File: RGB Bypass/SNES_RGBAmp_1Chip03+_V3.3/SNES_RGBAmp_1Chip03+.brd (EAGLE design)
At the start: 31.1 x 20.5 mm, 30 parts

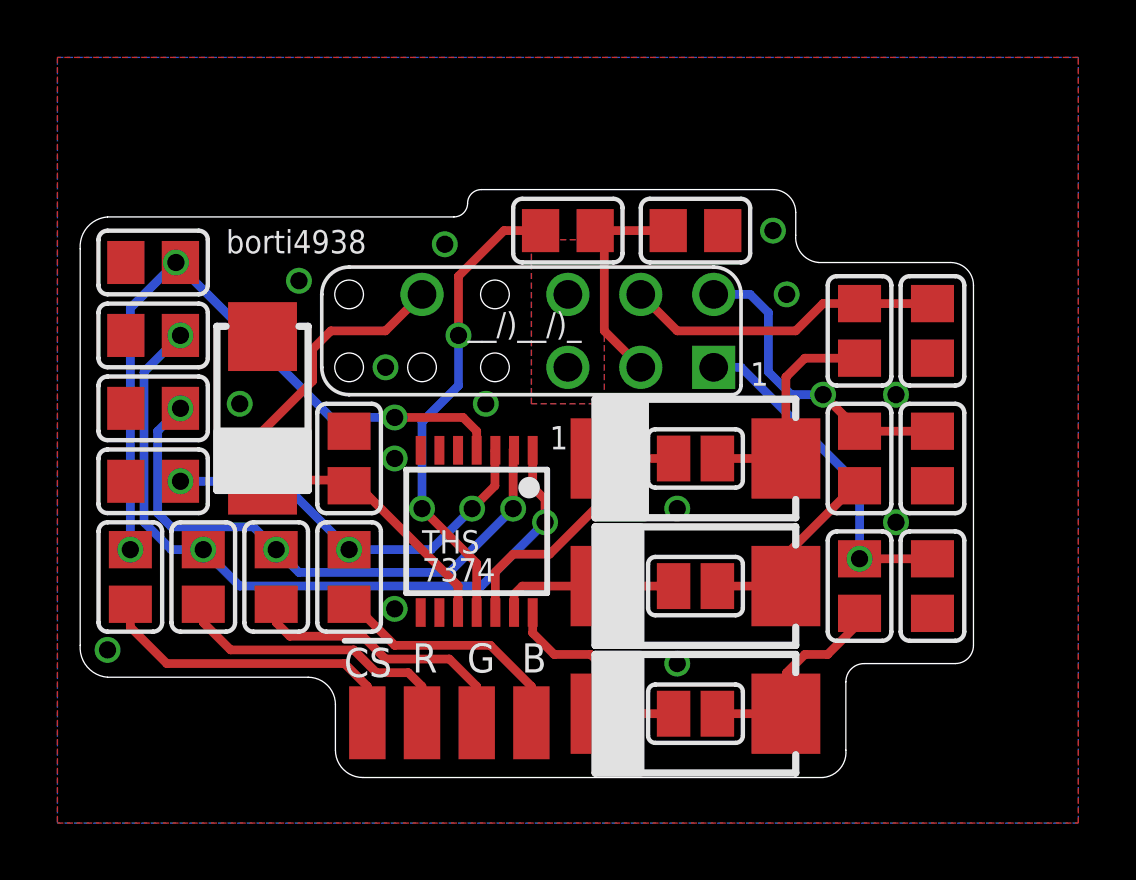
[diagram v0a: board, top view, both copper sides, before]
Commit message: Update: 330uF tantalum in CSYNC line at the output of the THS7374.
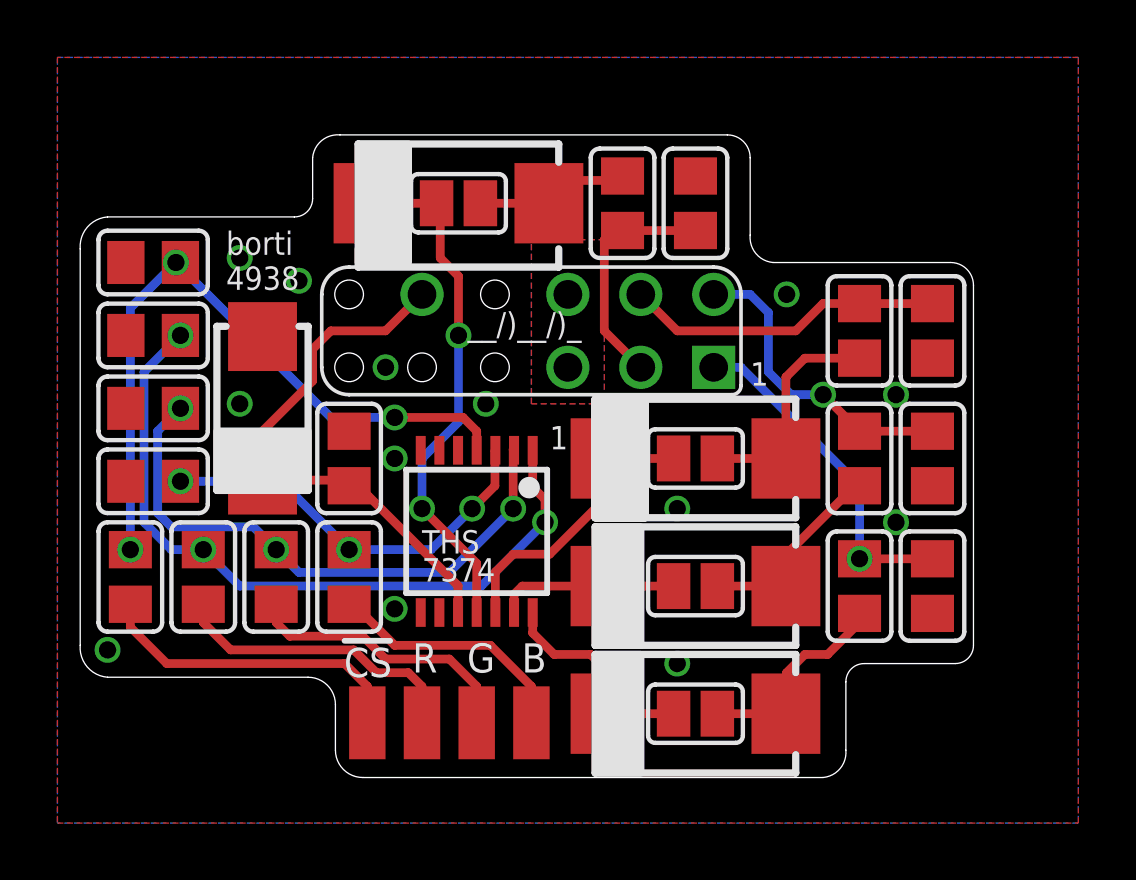
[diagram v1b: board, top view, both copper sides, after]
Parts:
- added C10: 330u, rcl:SMC_D
- added SJ4: (no value), jumper:SJ
- moved R15 2.13 mm to (29.8, 43.2), turned to 270 degrees
- moved C7 0.95 mm to (32.4, 43.2), turned to 90 degrees
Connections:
- new net N$19: C10.-, R15.1, SJ4.2
- net N$18: now also C10.+, SJ4.1; no longer R15.1
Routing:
- net N$19: track 0.00 -> 5.80 mm
- net N$18: track 16.5 -> 18.3 mm
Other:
- board size 31.1 x 20.5 mm -> 31.1 x 22.4 mm
- board text added: "C6 (330uF/ 6.3V )"
- board text added: "borti 4938"
- board text removed: "borti4938"

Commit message: Update silkscreen
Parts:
- removed R13, R14, R15: 75, snescart:Z0805
- added R7: 9.53k, snescart:Z0805
- added R8, R9: 8.45k, snescart:Z0805
- C10: value 330u -> 47p; device rcl:SMC_D -> snescart:Z0805
- C6: value 100n -> 330u; device snescart:Z0805 -> rcl:SMC_D
- C7, C8, C9: value 100n -> 47p
- R10: value 75 -> 75-421
- R11: value 75 -> 5.0k
- R12: value 75 -> 4.3k
- R4: value 75 -> 806
- R5, R6: value 75 -> 1.3k
- moved C6 21.2 mm to (24.1, 43.2), turned to 0 degrees
- moved R10 19.6 mm to (29.8, 43.2)
- moved C7 15.7 mm to (40.6, 29.8), turned to 270 degrees
- moved R12 12.9 mm to (13.5, 41.1), turned to 0 degrees
- moved R6 10.8 mm to (20.3, 30.2), turned to 270 degrees
- moved R1 8.89 mm to (38.1, 29.8)
- moved C10 8.25 mm to (32.4, 43.2), turned to 90 degrees
- moved R5 7.27 mm to (17.8, 30.2), turned to 270 degrees
- moved R11 5.08 mm to (12.7, 30.2)
- moved R2 4.45 mm to (38.1, 34.3)
- moved R3 4.45 mm to (38.1, 38.7)
- moved R4 3.76 mm to (15.2, 30.2), turned to 270 degrees
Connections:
- removed net N$3: R12.1, R4.2, U$2.3
- new net R9: R6.1, R9.2, U$2.3
- net GND: now also C10.2, R12.1, R7.1, R8.1, R9.1; no longer C6.2, R14.1, R4.1, R5.1, R6.1
- net N$1: now also R4.1, R7.2; no longer R10.1, R6.2
- net N$10: now also R11.1, R12.2; no longer R13.1, R14.2
- net N$13: now also R2.1; no longer R3.1
- net N$14: now also R4.2; no longer R10.2
- net N$15: now also R5.2; no longer R11.2
- net N$16: now also R6.2; no longer R12.2
- net N$17: now also R11.2; no longer R13.2
- net N$18: now also C6.+; no longer C10.+
- net N$19: now also C6.-, R10.1; no longer C10.-, R15.1
- net N$2: now also R5.1, R8.2; no longer R11.1, R5.2
- net N$20: now also C10.1, R10.2; no longer C7.1, R15.2
- net N$4: now also R1.1; no longer R2.1
- net N$5: now also C7.1, R1.2; no longer C6.1, R2.2
- net N$6: now also R2.2; no longer R3.2
- net N$8: now also R3.1; no longer R1.1
- net N$9: now also R3.2; no longer R1.2
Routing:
- net R9: track 0.00 -> 14.8 mm, vias 0 -> 3
- net N$3: track 14.8 -> 0.00 mm, vias 3 -> 0
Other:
- board text added: "(75Ω- 421Ω)"
- board text added: "+"
- board text removed: "(75Ω- 300Ω)"

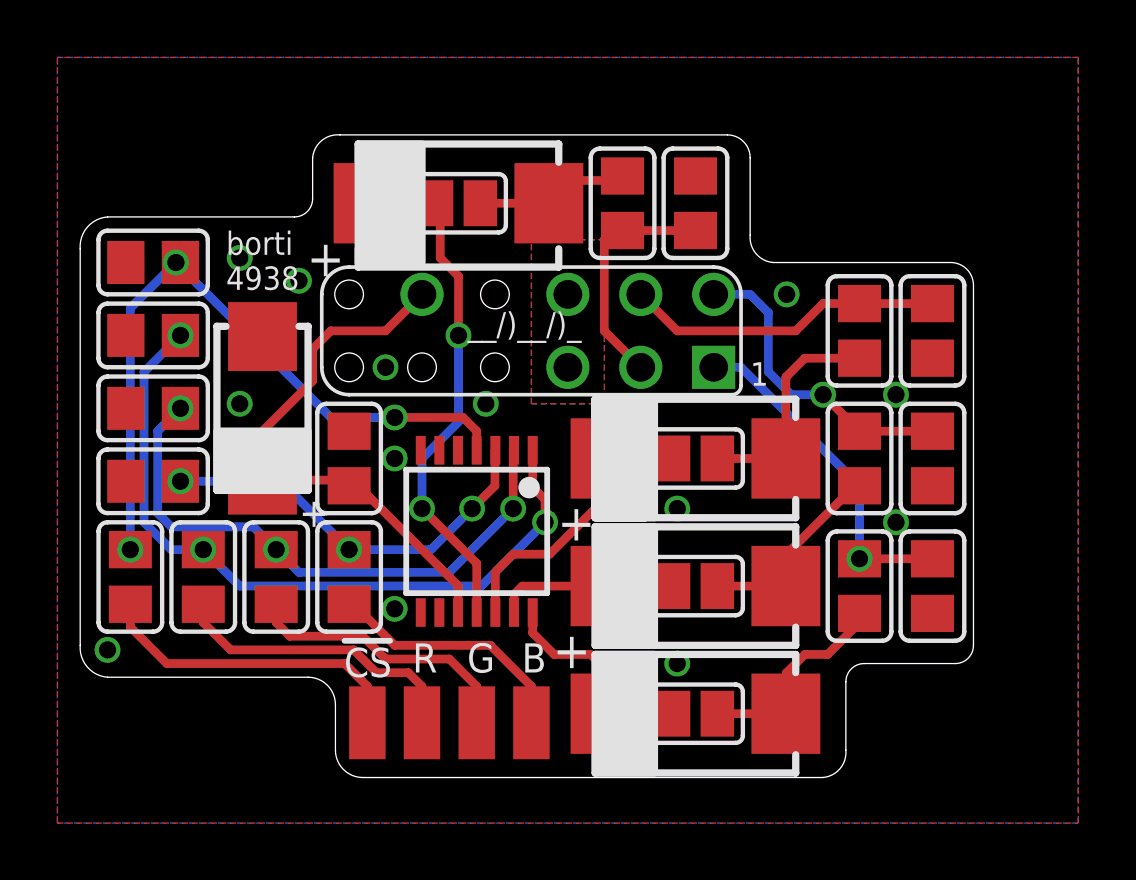
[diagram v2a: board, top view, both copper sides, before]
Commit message: move R12 to avoid a slight overlapping between the PCB and a mounting screw in SNES Mini and SFC Jr.
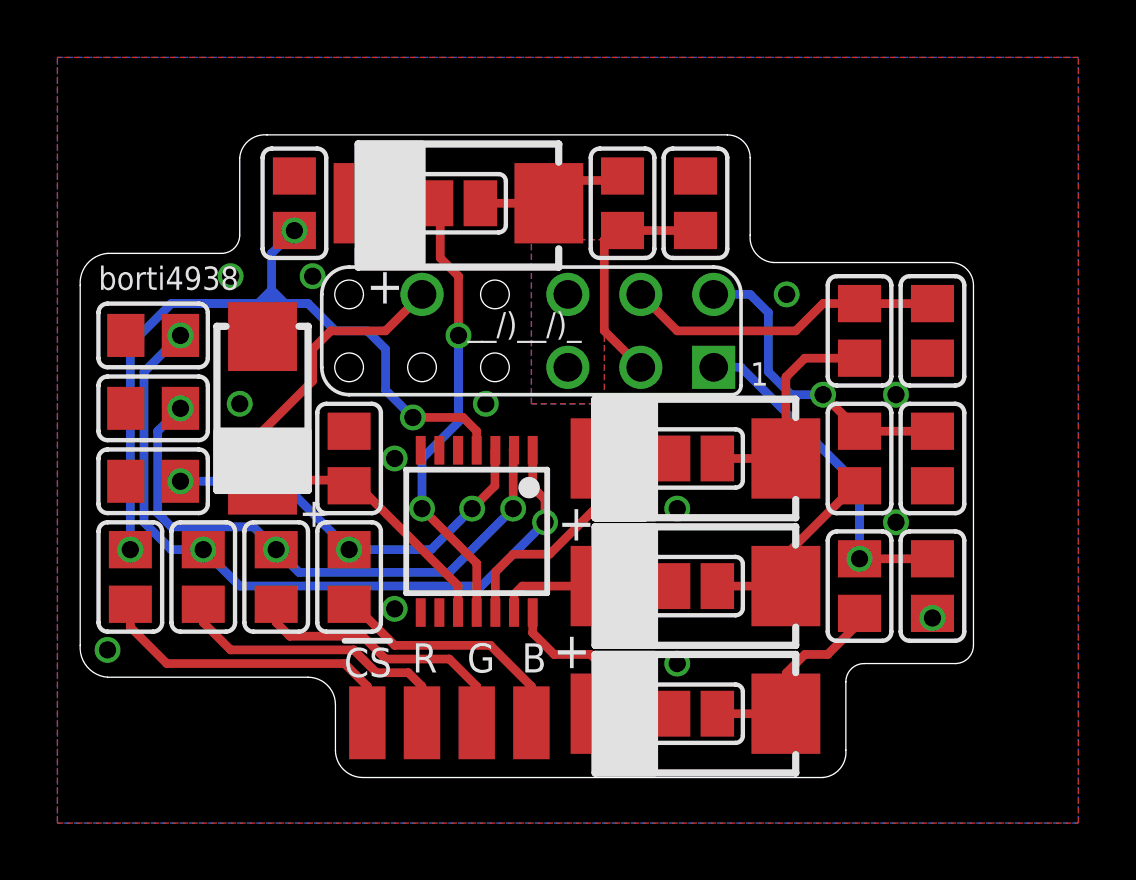
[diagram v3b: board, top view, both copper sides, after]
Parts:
- moved R12 5.34 mm to (18.4, 43.2), turned to 270 degrees
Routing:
- net N$10: track 24.6 -> 27.6 mm
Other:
- outline, holes or cut-outs redrawn
- board text added: "borti4938"
- board text removed: "borti 4938"
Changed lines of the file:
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@@
 <text x="30.95625" y="33.9725" size="1.016" layer="22" font="vector" ratio="12" rot="MR0">RGBAmp for
 SNES V3.3b</text>
-<wire x1="11.90625" y1="42.70375" x2="10.95375" y2="41.5925" width="0" layer="20" curve="90"/>
-<wire x1="10.95375" y1="41.5925" x2="10.95375" y2="27.78125" width="0" layer="20"/>
+<wire x1="11.90625" y1="41.43375" x2="10.95375" y2="40.3225" width="0" layer="20" curve="90"/>
+<wire x1="10.95375" y1="40.3225" x2="10.95375" y2="27.78125" width="0" layer="20"/>
 <wire x1="10.95375" y1="27.78125" x2="11.90625" y2="26.67" width="0" layer="20" curve="90"/>
 <wire x1="11.90625" y1="26.67" x2="18.89125" y2="26.67" width="0" layer="20"/>
@@
 <wire x1="41.43375" y1="27.14625" x2="42.06875" y2="27.78125" width="0" layer="20" curve="90"/>
 <text x="18.57375" y="31.90875" size="1.016" layer="21" font="vector" ratio="15" distance="20">+</text>
-<wire x1="11.90625" y1="42.70375" x2="18.415" y2="42.70375" width="0" layer="20"/>
-<wire x1="20.0025" y1="45.56125" x2="33.49625" y2="45.56125" width="0" layer="20"/>
+<wire x1="11.90625" y1="41.43375" x2="15.875" y2="41.43375" width="0" layer="20"/>
+<wire x1="17.4625" y1="45.56125" x2="33.49625" y2="45.56125" width="0" layer="20"/>
 <wire x1="33.49625" y1="45.56125" x2="34.29" y2="44.7675" width="0" layer="20" curve="-90"/>
 <wire x1="34.29" y1="44.7675" x2="34.29" y2="42.06875" width="0" layer="20"/>
@@
 <text x="30.00375" y="42.06875" size="0.8128" layer="26" font="vector" ratio="15" distance="20" rot="MR90">R10</text>
 <text x="12.85875" y="28.73375" size="0.8128" layer="26" font="vector" ratio="15" distance="20" rot="MR90">R11</text>
-<text x="13.97" y="41.275" size="0.8128" layer="26" font="vector" ratio="15" distance="20" rot="MR0">R12</text>
-<text x="15.5575" y="40.16375" size="0.8128" layer="26" font="vector" ratio="15" distance="20" rot="MR0">(4.3kΩ)</text>
+<text x="18.57375" y="42.70375" size="0.8128" layer="26" font="vector" ratio="15" distance="20" rot="MR90">R12</text>
+<text x="17.4625" y="41.11625" size="0.8128" layer="26" font="vector" ratio="15" distance="20" rot="MR90">(4.3kΩ)</text>
 <text x="11.7475" y="28.09875" size="0.8128" layer="26" font="vector" ratio="15" distance="20" rot="MR90">(5.0kΩ)</text>
 <wire x1="20.16125" y1="27.94" x2="21.74875" y2="27.94" width="0.2032" layer="25"/>
-<wire x1="18.415" y1="42.70375" x2="19.05" y2="43.33875" width="0" layer="20" curve="90"/>
-<text x="16.03375" y="40.16375" size="0.8128" layer="21" font="vector" ratio="15">borti
-4938</text>
+<wire x1="15.875" y1="41.43375" x2="16.51" y2="42.06875" width="0" layer="20" curve="90"/>
 <text x="14.44625" y="28.2575" size="0.8128" layer="26" font="vector" ratio="15" distance="20" rot="MR90">(806Ω)</text>
 <text x="12.065" y="32.385" size="0.8128" layer="26" font="vector" ratio="15" distance="20" rot="MR90">(8.45kΩ)</text>
@@
 <text x="27.94" y="41.43375" size="0.8128" layer="26" font="vector" ratio="15" distance="20" rot="MR90">(75Ω-
 421Ω)</text>
-<wire x1="19.05" y1="43.33875" x2="19.05" y2="44.7675" width="0" layer="20"/>
-<wire x1="19.05" y1="44.7675" x2="20.0025" y2="45.56125" width="0" layer="20" curve="-90"/>
+<wire x1="16.51" y1="42.06875" x2="16.51" y2="44.7675" width="0" layer="20"/>
+<wire x1="16.51" y1="44.7675" x2="17.4625" y2="45.56125" width="0" layer="20" curve="-90"/>
 <text x="26.51125" y="41.91" size="0.8128" layer="26" font="vector" ratio="15" distance="20" rot="MR0">  C6
 (330uF/
@@
 <text x="28.73375" y="28.2575" size="1.27" layer="21" font="vector" ratio="15" distance="20" rot="R180">+</text>
 <text x="28.8925" y="32.7025" size="1.27" layer="21" font="vector" ratio="15" distance="20" rot="R180">+</text>
-<text x="20.16125" y="41.91" size="1.27" layer="21" font="vector" ratio="15" distance="20" rot="R180">+</text>
-<wire x1="15.39875" y1="41.91" x2="15.08125" y2="42.2275" width="0.1524" layer="22" curve="90"/>
-<wire x1="15.08125" y1="42.2275" x2="11.90625" y2="42.2275" width="0.1524" layer="22"/>
-<wire x1="11.90625" y1="42.2275" x2="11.58875" y2="41.91" width="0.1524" layer="22" curve="90"/>
-<wire x1="11.58875" y1="41.91" x2="11.58875" y2="41.11625" width="0.1524" layer="22"/>
-<wire x1="11.7475" y1="40.005" x2="15.24" y2="40.005" width="0.1524" layer="22"/>
-<wire x1="15.39875" y1="41.11625" x2="15.39875" y2="41.91" width="0.1524" layer="22"/>
+<text x="22.225" y="40.9575" size="1.27" layer="21" font="vector" ratio="15" distance="20" rot="R180">+</text>
+<wire x1="19.20875" y1="41.275" x2="19.52625" y2="41.5925" width="0.1524" layer="22" curve="90"/>
+<wire x1="19.52625" y1="41.5925" x2="19.52625" y2="44.7675" width="0.1524" layer="22"/>
+<wire x1="19.52625" y1="44.7675" x2="19.20875" y2="45.085" width="0.1524" layer="22" curve="90"/>
+<wire x1="19.20875" y1="45.085" x2="18.415" y2="45.085" width="0.1524" layer="22"/>
+<wire x1="17.30375" y1="44.92625" x2="17.30375" y2="41.43375" width="0.1524" layer="22"/>
+<wire x1="18.415" y1="41.275" x2="19.20875" y2="41.275" width="0.1524" layer="22"/>
 <wire x1="11.58875" y1="38.57625" x2="11.58875" y2="39.37" width="0.1524" layer="22"/>
 <wire x1="11.58875" y1="39.37" x2="11.90625" y2="39.6875" width="0.1524" layer="22" curve="-90"/>
@@
 <wire x1="33.9725" y1="40.005" x2="33.02" y2="40.9575" width="0.1524" layer="22" curve="90"/>
 <wire x1="33.02" y1="40.9575" x2="20.16125" y2="40.9575" width="0.1524" layer="22"/>
+<text x="11.58875" y="40.16375" size="0.8128" layer="21" font="vector" ratio="15">borti4938</text>
 </plain>
 <attributes>
@@
 <attribute name="NAME" x="20.1425" y="26.67625" size="1.016" layer="25" font="vector" ratio="12"/>
 </element>
-<element name="R12" library="snescart" package="Z0805" value="4.3k" x="13.49375" y="41.11625" smashed="yes"/>
+<element name="R12" library="snescart" package="Z0805" value="4.3k" x="18.415" y="43.18" smashed="yes" rot="R270"/>
 <element name="R10" library="snescart" package="Z0805" value="75-421" x="29.845" y="43.18" smashed="yes" rot="R270"/>
 <element name="C10" library="snescart" package="Z0805" value="47p" x="32.385" y="43.18" smashed="yes" rot="R90"/>
@@
 </polygon>
 <via x="31.75" y="27.14625" extent="1-16" drill="0.6"/>
-<via x="21.59" y="37.465" extent="1-16" drill="0.6"/>
+<via x="19.05" y="40.64" extent="1-16" drill="0.6"/>
 <via x="31.75" y="32.54375" extent="1-16" drill="0.6"/>
 <contactref element="U$3" pad="P$6"/>
@@
 <via x="25.0825" y="36.195" extent="1-16" drill="0.6"/>
 <via x="35.56" y="40.005" extent="1-16" drill="0.6"/>
-<via x="18.57375" y="40.48125" extent="1-16" drill="0.6"/>
 <via x="16.51" y="36.195" extent="1-16" drill="0.6"/>
 <via x="11.90625" y="27.6225" extent="1-16" drill="0.6"/>
-<via x="16.51" y="41.275" extent="1-16" drill="0.6"/>
+<via x="16.1925" y="40.64" extent="1-16" drill="0.6"/>
 <contactref element="C7" pad="2"/>
 <contactref element="C8" pad="2"/>
@@
 <via x="39.37" y="32.0675" extent="1-16" drill="0.6"/>
 <via x="39.37" y="36.5125" extent="1-16" drill="0.6"/>
+<via x="40.64" y="28.73375" extent="1-16" drill="0.6"/>
 </signal>
 <signal name="VCC">
@@
 <contactref element="R12" pad="2"/>
 <contactref element="R11" pad="1"/>
-<wire x1="14.2875" y1="41.11375" x2="14.44375" y2="41.11625" width="0.3048" layer="1"/>
 <wire x1="12.7" y1="31.1125" x2="12.7" y2="31.115" width="0.3048" layer="1"/>
 <via x="12.7" y="31.115" extent="1-16" drill="0.6"/>
-<via x="14.2875" y="41.11625" extent="1-16" drill="0.6"/>
-<wire x1="14.2875" y1="41.11625" x2="14.2875" y2="41.11875" width="0.3048" layer="1"/>
-<wire x1="14.2875" y1="41.11875" x2="14.44375" y2="41.11625" width="0.3048" layer="1"/>
-<wire x1="14.2875" y1="41.11625" x2="12.7" y2="39.52875" width="0.3048" layer="16"/>
-<wire x1="12.7" y1="39.52875" x2="12.7" y2="31.115" width="0.3048" layer="16"/>
-<via x="21.9075" y="35.71875" extent="1-16" drill="0.6"/>
-<wire x1="21.9075" y1="35.71875" x2="19.685" y2="35.71875" width="0.3048" layer="16"/>
-<wire x1="19.685" y1="35.71875" x2="14.2875" y2="41.11625" width="0.3048" layer="16"/>
-<wire x1="21.9075" y1="35.71875" x2="24.28875" y2="35.71875" width="0.3048" layer="1"/>
+<wire x1="18.415" y1="42.2275" x2="18.4175" y2="42.38625" width="0.3048" layer="1"/>
+<wire x1="12.7" y1="38.25875" x2="12.7" y2="31.115" width="0.3048" layer="16"/>
+<via x="22.5425" y="35.71875" extent="1-16" drill="0.6"/>
+<wire x1="22.5425" y1="35.71875" x2="24.28875" y2="35.71875" width="0.3048" layer="1"/>
 <wire x1="24.28875" y1="35.71875" x2="24.765" y2="35.2425" width="0.3048" layer="1"/>
 <wire x1="24.765" y1="35.2425" x2="24.765" y2="34.575" width="0.3048" layer="1"/>
+<wire x1="12.7" y1="38.25875" x2="14.12875" y2="39.6875" width="0.3048" layer="16"/>
+<wire x1="20.955" y1="38.735" x2="21.59" y2="38.1" width="0.3048" layer="16"/>
+<wire x1="21.59" y1="38.1" x2="21.59" y2="36.67125" width="0.3048" layer="16"/>
+<wire x1="21.59" y1="36.67125" x2="22.5425" y2="35.71875" width="0.3048" layer="16"/>
+<via x="18.415" y="42.2275" extent="1-16" drill="0.6"/>
+<wire x1="18.415" y1="42.23" x2="18.415" y2="42.2275" width="0.3048" layer="1"/>
+<wire x1="20.955" y1="38.735" x2="19.84375" y2="38.735" width="0.3048" layer="16"/>
+<wire x1="19.84375" y1="38.735" x2="18.89125" y2="39.6875" width="0.3048" layer="16"/>
+<wire x1="14.12875" y1="39.6875" x2="17.145" y2="39.6875" width="0.3048" layer="16"/>
+<wire x1="17.145" y1="39.6875" x2="17.62125" y2="40.16375" width="0.3048" layer="16"/>
+<wire x1="17.62125" y1="40.16375" x2="18.0975" y2="39.6875" width="0.3048" layer="16"/>
+<wire x1="18.0975" y1="39.6875" x2="17.4625" y2="39.6875" width="0.3048" layer="16"/>
+<wire x1="17.145" y1="39.6875" x2="17.4625" y2="39.6875" width="0.3048" layer="16"/>
+<wire x1="17.4625" y1="39.6875" x2="17.62125" y2="39.84625" width="0.3048" layer="16"/>
+<wire x1="17.62125" y1="39.84625" x2="17.62125" y2="41.43375" width="0.3048" layer="16"/>
+<wire x1="17.62125" y1="41.43375" x2="18.415" y2="42.2275" width="0.3048" layer="16"/>
+<wire x1="18.89125" y1="39.6875" x2="18.0975" y2="39.6875" width="0.3048" layer="16"/>
 </signal>
 <signal name="N$17">
